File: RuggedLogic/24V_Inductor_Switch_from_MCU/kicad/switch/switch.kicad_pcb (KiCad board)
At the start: 2 copper layers, 52.3 x 50.8 mm, 17 parts

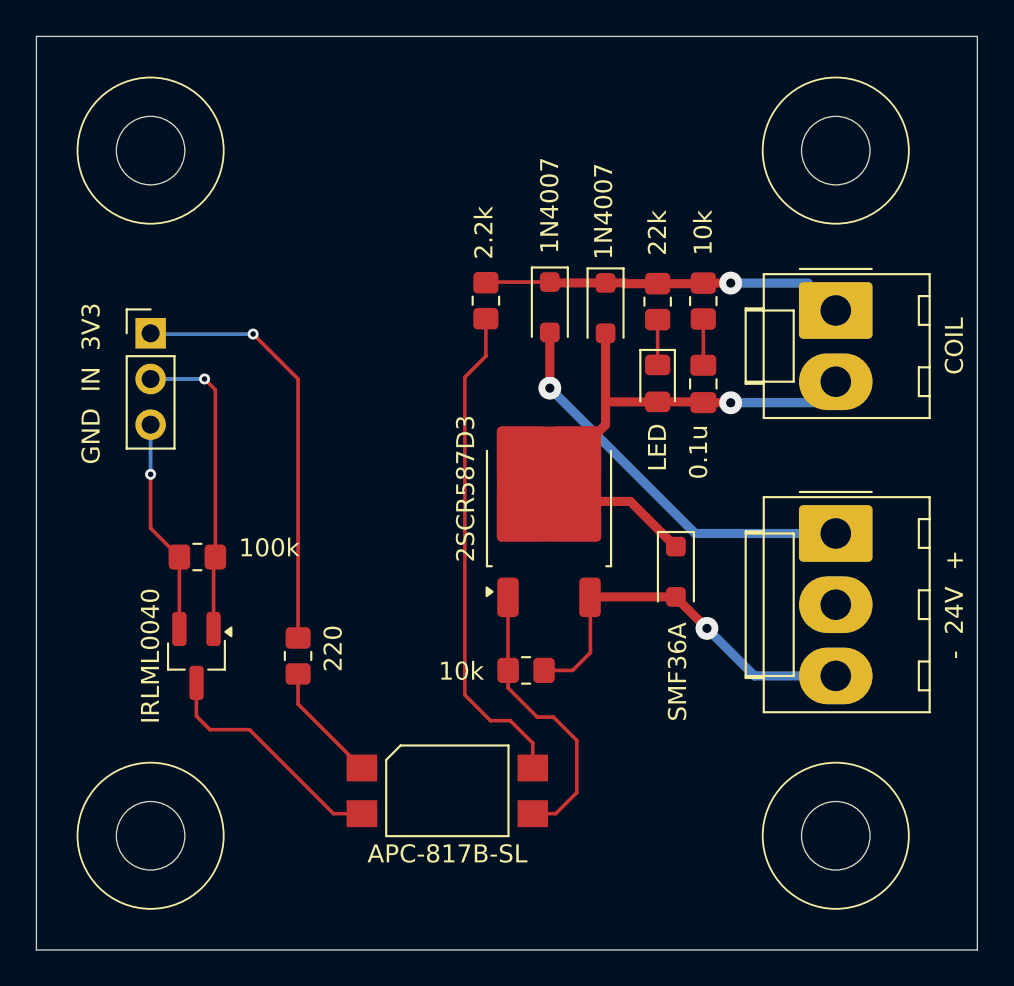
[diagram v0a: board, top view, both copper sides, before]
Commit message: Redone Z-input PCB; production update
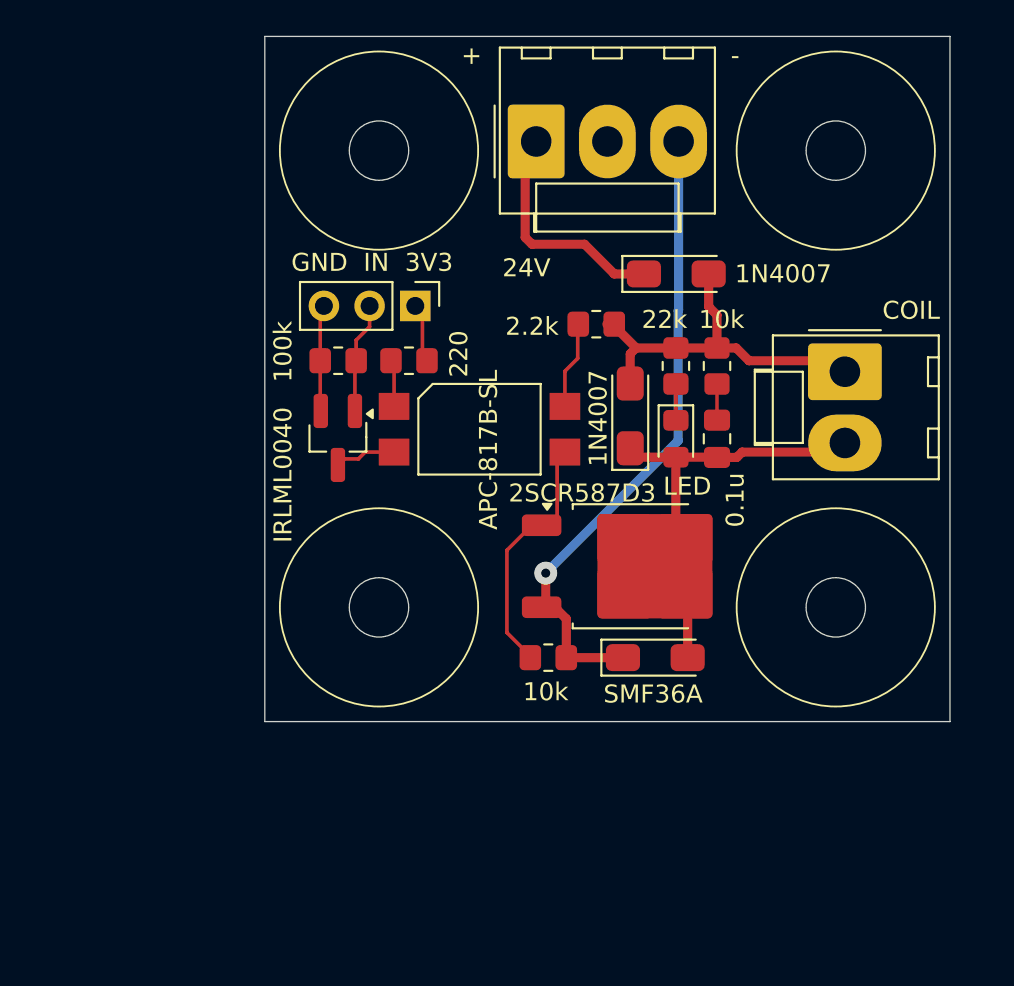
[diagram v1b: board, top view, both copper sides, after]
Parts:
- 1N4007 (x2), SMF36A: footprint Secoh:D_SOD-123F_inverted_polarity -> Secoh:D_SOD-123F_hand_soldering
- moved -  24V  + 27.4 mm to (84.9, 24.9), turned to 0 degrees
- moved APC-817B-SL 20.2 mm to (81.8, 40.9)
- moved 220 17.5 mm to (77.9, 37.1), turned to 0 degrees
- moved GND  IN  3V3 14.8 mm to (78.2, 34.0), turned to -90 degrees
- moved IRLML0040 14.4 mm to (73.9, 41.4)
- moved 100k 13.4 mm to (73.9, 37.1)
- moved 1N4007 7.27 mm to (92.7, 32.3), turned to 0 degrees
- moved 2.2k 6.27 mm to (88.3, 35.1), turned to 0 degrees
- moved 1N4007 6.15 mm to (90.2, 40.2), turned to 90 degrees
- moved 2SCR587D3 5.69 mm to (90.3, 48.5), turned to 0 degrees
- moved SMF36A 4.91 mm to (91.6, 53.6), turned to 0 degrees
- moved 22k 3.72 mm to (92.7, 37.4)
- moved 10k 3.69 mm to (95.0, 37.4)
- moved COIL 3.44 mm to (102.1, 37.7)
- moved LED 3.24 mm to (92.7, 41.4)
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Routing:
- net Net-(D5-C-Pad4): track 27.7 -> 5.02 mm
- net Net-(J3-Pin_1): track 23.7 -> 3.32 mm, vias 1 -> 0
- net GNO-O: track 21.6 -> 36.0 mm
- net Net-(J3-Pin_2): track 17.2 -> 6.18 mm, vias 1 -> 0
- net Net-(D5-D-): track 13.3 -> 3.42 mm
- net 24V: track 22.3 -> 13.0 mm, vias 1 -> 0
- net OUT: track 27.5 -> 20.8 mm, vias 1 -> 0
- net Net-(J3-Pin_3): track 12.0 -> 5.94 mm, vias 1 -> 0
- net Net-(D5-D+): track 6.70 -> 2.61 mm
- net Net-(T2-B): track 15.9 -> 14.1 mm
- net 24V_a: track 20.2 -> 20.8 mm, vias 1 -> 0
- net Net-(C3-Pad1): track 2.57 -> 2.01 mm
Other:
- board size 52.3 x 50.8 mm -> 38.1 x 38.1 mm
- board text added: "+"
- board text added: "-"
- board text added: "24V"
- board text added: "JLCJLCJLCJLC"

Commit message: Fixed errors in Rugged Z sensor Fixes to Rugged Switch
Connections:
- net 24V renamed /24V
- net 24V_a renamed /24V_O
- net GNO-O renamed /GND_O
- net Net-(J3-Pin_1) renamed /3V3
- net Net-(J3-Pin_2) renamed /IN
- net Net-(J3-Pin_3) renamed /GND_I
- net OUT renamed /OUT

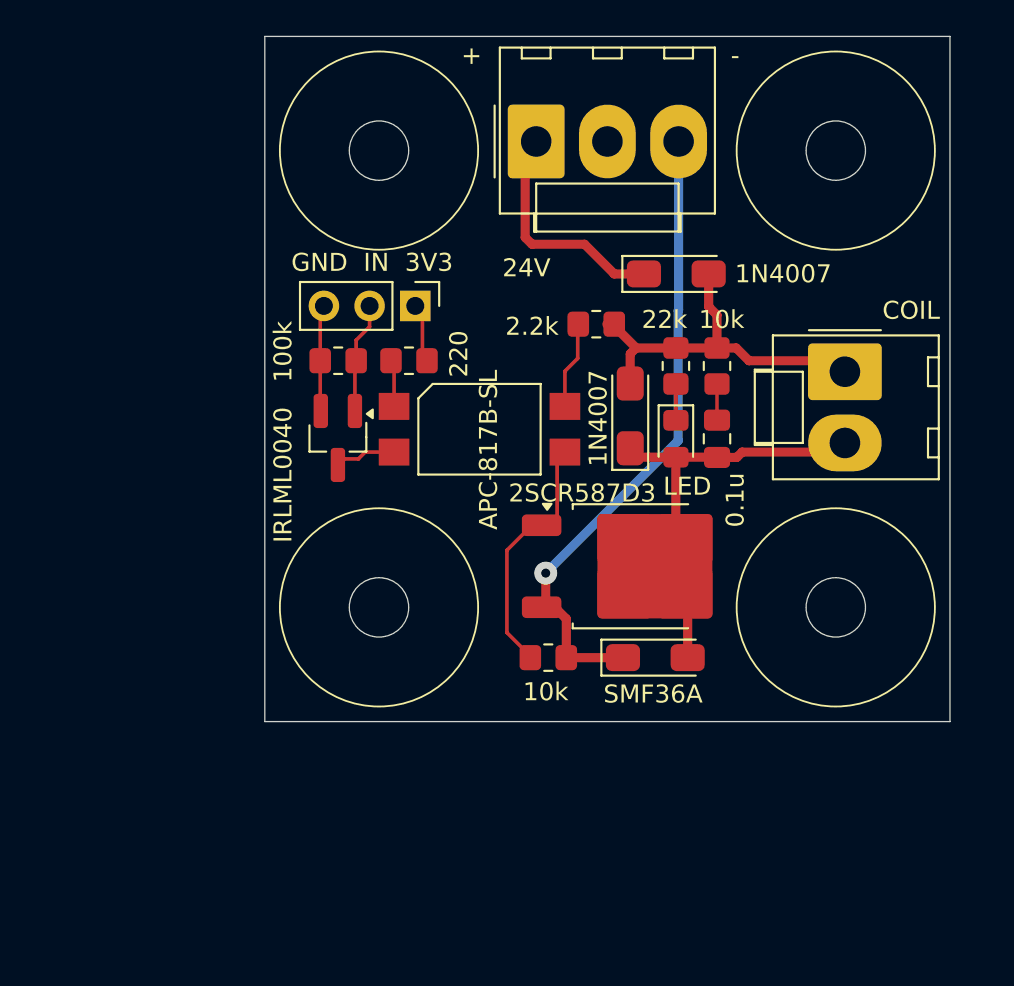
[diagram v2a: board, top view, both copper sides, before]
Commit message: Updated Rugged Z sensor and Switch; schematics and PCB
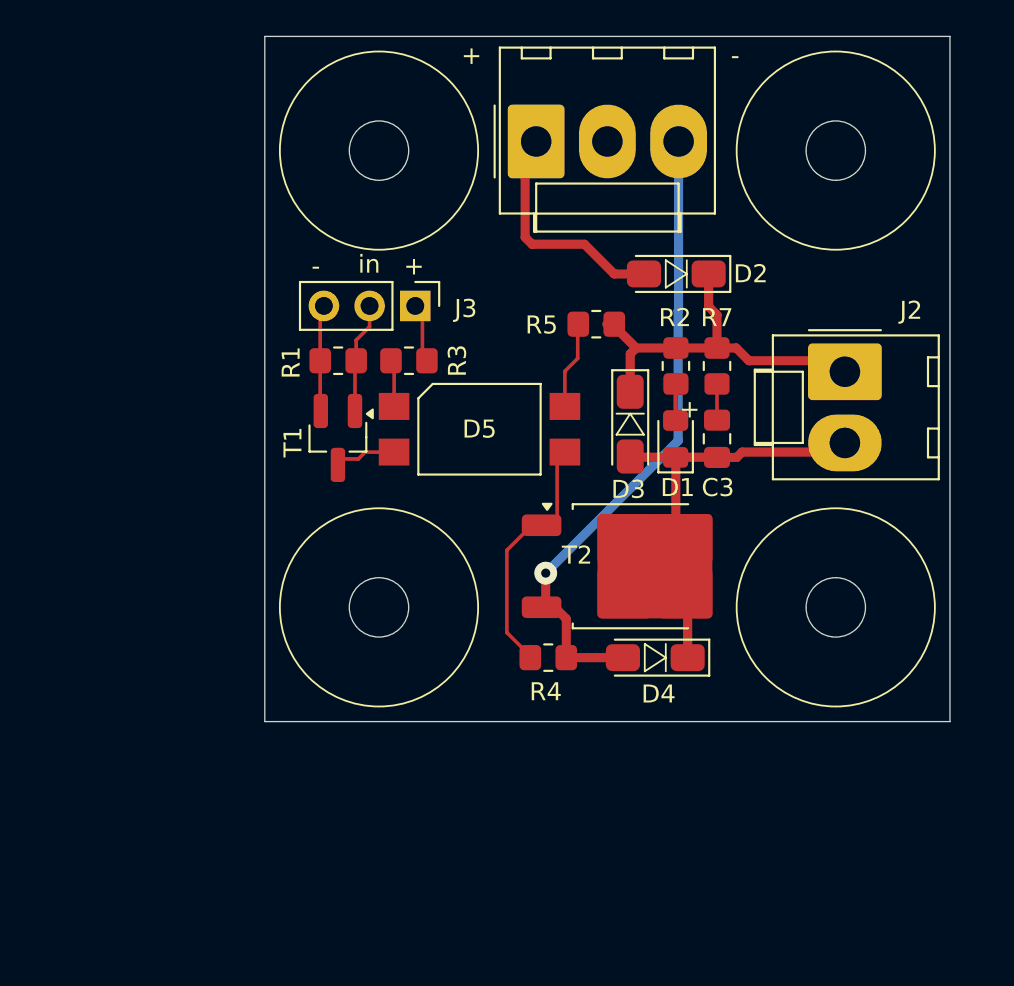
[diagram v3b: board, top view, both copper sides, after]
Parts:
- D1: renamed from LED; footprint LED_SMD:LED_0805_2012Metric_Pad1.15x1.40mm_HandSolder -> Secoh:LED_0805
- D5: renamed from APC-817B-SL; value APC-817B-SL -> PC817B
- J1: renamed from -  24V  +
- J2: renamed from COIL; value COIL -> Conn_01x02_Pin
- J3: renamed from GND  IN  3V3; value GND IN 3V3 -> Conn_01x03_Pin
- moved D3 0.46 mm to (90.2, 40.6), turned to -90 degrees
- turned D1 to 90 degrees
- turned D2 to 180 degrees
- turned D4 to 180 degrees
- renumbered 0.1u to C3, 1N4007 to D2, 1N4007 to D3, SMF36A to D4, 100k to R1, 22k to R2, 220 to R3, 10k to R4, 2.2k to R5, 10k to R7, IRLML0040 to T1, 2SCR587D3 to T2
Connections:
- net /3V3 renamed Net-(J3-Pin_1)
- net /GND_I renamed Net-(J3-Pin_3)
- net /IN renamed Net-(J3-Pin_2)
- C3 pad 2: /OUT -> Net-(D1-K)
- D1 pad 1: Net-(D1-+) -> Net-(D1-K)
- D1 pad 2: /OUT -> Net-(D1-A)
- D2 pad 1: /24V -> Net-(D2-K)
- D2 pad 2: /24V_O -> Net-(D2-A)
- D3 pad 1: /OUT -> Net-(D2-K)
- D3 pad 2: /24V_O -> Net-(D1-K)
- D4 pad 1: /GND_O -> Net-(D1-K)
- D4 pad 2: /OUT -> Net-(D4-A)
- J1 pad 1: /24V -> Net-(D2-A)
- J1 pad 3: /GND_O -> Net-(D4-A)
- J2 pad 1: /24V_O -> Net-(D2-K)
- J2 pad 2: /OUT -> Net-(D1-K)
- R2 pad 1: Net-(D1-+) -> Net-(D1-A)
- R2 pad 2: /24V_O -> Net-(D2-K)
- R4 pad 1: /GND_O -> Net-(D4-A)
- R5 pad 2: /24V_O -> Net-(D2-K)
- R7 pad 2: /24V_O -> Net-(D2-K)
- T2 pad 2: /OUT -> Net-(D1-K)
- T2 pad 3: /GND_O -> Net-(D4-A)
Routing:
- net /GND_O: track 36.0 -> 0.00 mm, vias 1 -> 0
- net Net-(D4-A): track 0.00 -> 36.0 mm, vias 0 -> 1
- net /OUT: track 20.8 -> 0.00 mm
- net Net-(D1-K): track 0.00 -> 20.8 mm
- net /24V_O: track 20.8 -> 0.00 mm
- net Net-(D2-K): track 0.00 -> 20.8 mm
- net /24V: track 13.0 -> 0.00 mm
- net Net-(D2-A): track 0.00 -> 13.0 mm
- net Net-(D1-A): track 0.00 -> 2.02 mm
- net Net-(D1-+): track 2.02 -> 0.00 mm
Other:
- board text added: "in"
- board text removed: "24V"
